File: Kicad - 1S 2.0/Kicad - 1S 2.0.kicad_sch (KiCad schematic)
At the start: 25 parts, among them J1 HRO_TYPE_C_31_M_12, J2 Conn_01x02, SW1 SW_SPDT, U1 BQ24074RGT, U2 TLV62569DBV

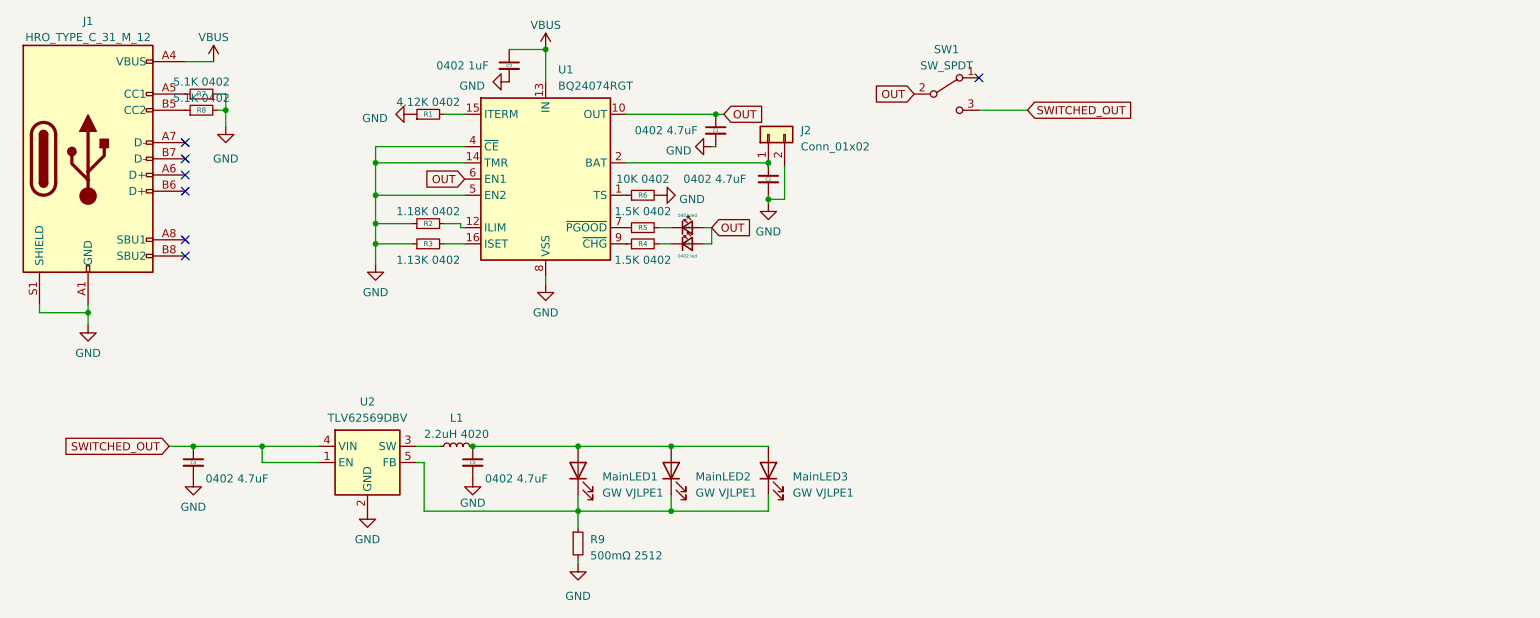
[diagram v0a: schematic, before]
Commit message: changed LEDs over to a standard format to make the board cheaper
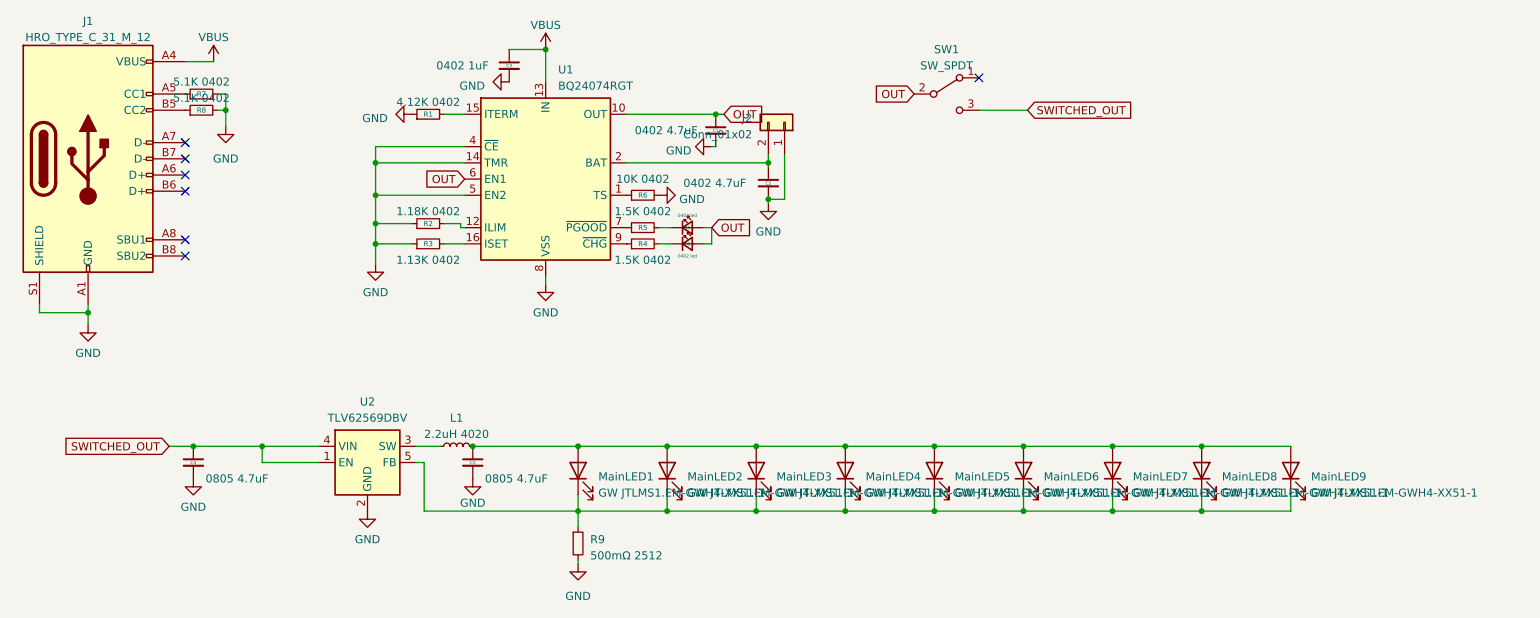
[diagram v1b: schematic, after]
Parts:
- added MainLED4, MainLED5, MainLED6, MainLED7, MainLED8, MainLED9: GW JTLMS1.EM-GWH4-XX51-1, LED_SMD:LED_PLCC_2835, symbol Device:LED
- C4, C5: value 0402 4.7uF -> 0805 4.7uF; footprint Capacitor_SMD:C_0402_1005Metric -> Capacitor_SMD:C_0805_2012Metric
- MainLED1, MainLED2, MainLED3: value GW VJLPE1 -> GW JTLMS1.EM-GWH4-XX51-1; footprint VJLPE1:VJLPE1 -> LED_SMD:LED_PLCC_2835
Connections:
- net GND: now also J2.1 (Pin_1); no longer J2.2 (Pin_2)
- net at MainLED1.1 (K), MainLED2.1 (K), MainLED3.1 (K)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: now also MainLED4.1 (K), MainLED5.1 (K), MainLED6.1 (K), MainLED7.1 (K), MainLED8.1 (K), MainLED9.1 (K)
- net at C2.1, U1.2 (BAT), U1.3 (BAT): now also J2.2 (Pin_2); no longer J2.1 (Pin_1)
- net at C5.1, L1.2, MainLED1.2 (A)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: now also MainLED4.2 (A), MainLED5.2 (A), MainLED6.2 (A), MainLED7.2 (A), MainLED8.2 (A), MainLED9.2 (A)
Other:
- moved on the sheet: C2, J2
